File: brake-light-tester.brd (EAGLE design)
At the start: 160 x 100 mm, 24 parts, among them J1 CON_HEADER_PRG_AVR_ICSP-SMD, U1 ATTINY85-20SU, U2 TSL2561FN, U4 LM1117/5V

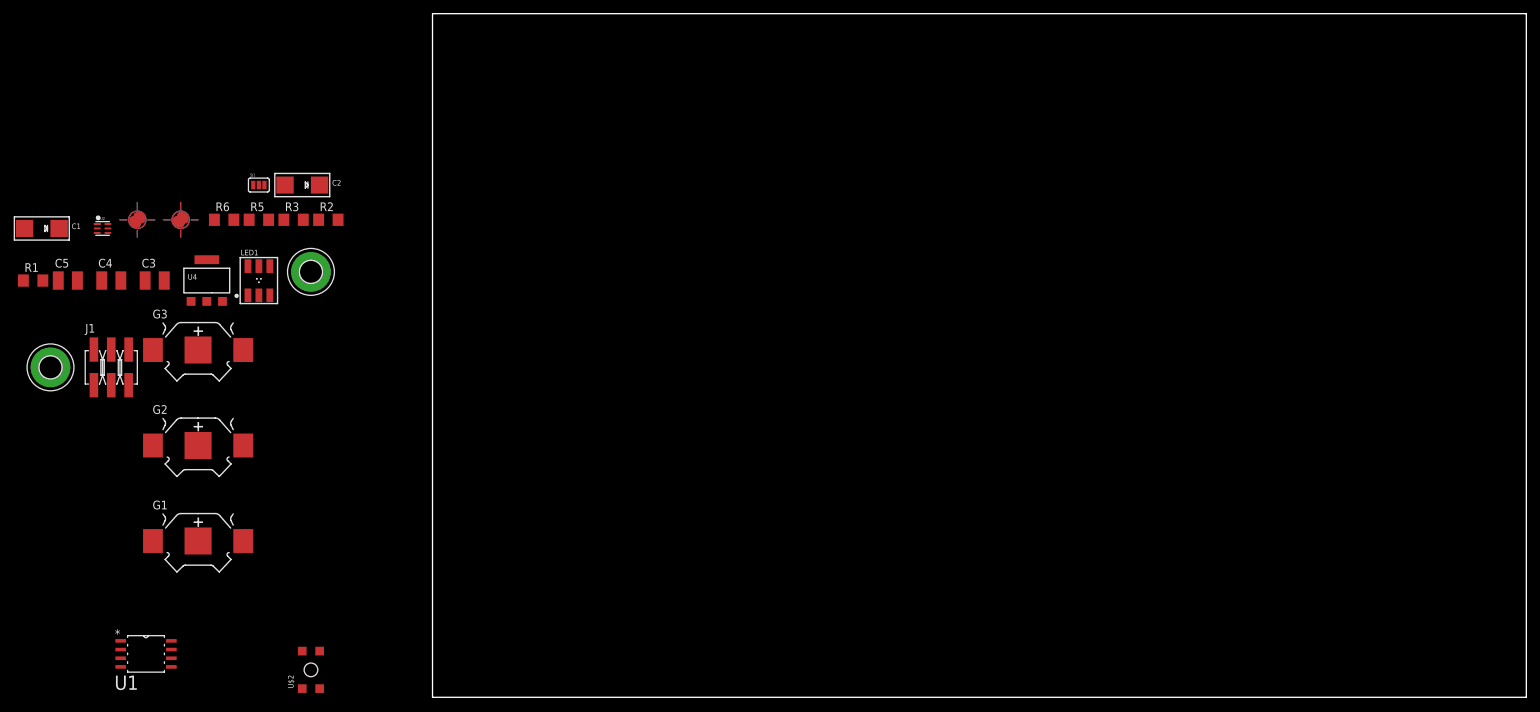
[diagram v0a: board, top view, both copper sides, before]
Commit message: Components laid out but unrouted.
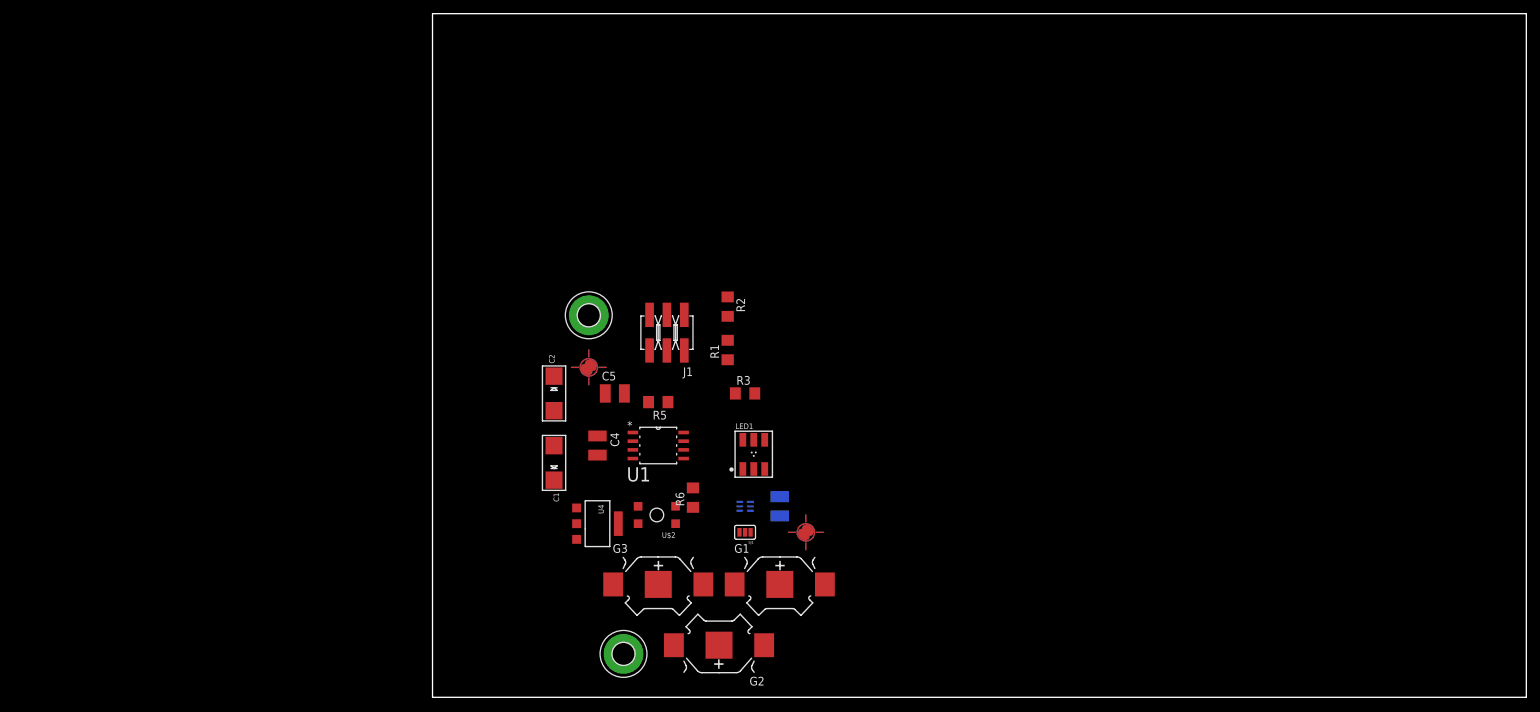
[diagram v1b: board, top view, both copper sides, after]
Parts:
- moved FID2 107.9 mm to (54.6, 24.1)
- moved U2 102.4 mm to (45.7, 27.9), flipped to the bottom
- moved R1 102.1 mm to (43.2, 50.8), turned to 90 degrees
- moved C3 97.2 mm to (50.8, 27.9), flipped to the bottom, turned to 270 degrees
- moved SJ1 87.4 mm to (45.7, 24.1), turned to 180 degrees
- moved G1 85.3 mm to (50.8, 16.5)
- moved C1 82.4 mm to (17.8, 34.3), turned to 270 degrees
- moved C5 81.7 mm to (26.7, 44.5)
- moved G2 81.6 mm to (41.9, 7.62), turned to 180 degrees
- moved J1 81.4 mm to (34.3, 53.3), turned to 180 degrees
- moved U1 80.9 mm to (33.0, 36.8)
- moved R6 79.7 mm to (38.1, 29.2), turned to 90 degrees
- moved H1 79.1 mm to (22.9, 55.9)
- moved LED1 76.7 mm to (47.0, 35.6)
- moved G3 75.5 mm to (33.0, 16.5)
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
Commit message: Manually routed PCB, first iteration.
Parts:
- moved FID2 0.94 mm to (54.8, 25.1)
- turned SJ1 to 0 degrees
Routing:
- net +5V: track 0.00 -> 121.5 mm, vias 0 -> 8
- net GND: track 0.00 -> 104.5 mm, vias 0 -> 5
- net PB2: track 0.00 -> 49.9 mm, vias 0 -> 3
- net PB0: track 0.00 -> 41.3 mm, vias 0 -> 3
- net N$1: track 0.00 -> 37.1 mm
- net PB1: track 0.00 -> 27.1 mm, vias 0 -> 2
- net N$6: track 0.00 -> 26.8 mm
- net N$5: track 0.00 -> 26.2 mm
- net PB5: track 0.00 -> 20.1 mm
- net PB4: track 0.00 -> 19.8 mm
- net N$3: track 0.00 -> 19.1 mm, vias 0 -> 2
- net PB3: track 0.00 -> 11.5 mm, vias 0 -> 2
- net N$2: track 0.00 -> 7.57 mm, vias 0 -> 1
- net N$4: track 0.00 -> 6.84 mm
- net N$7: track 0.00 -> 2.60 mm

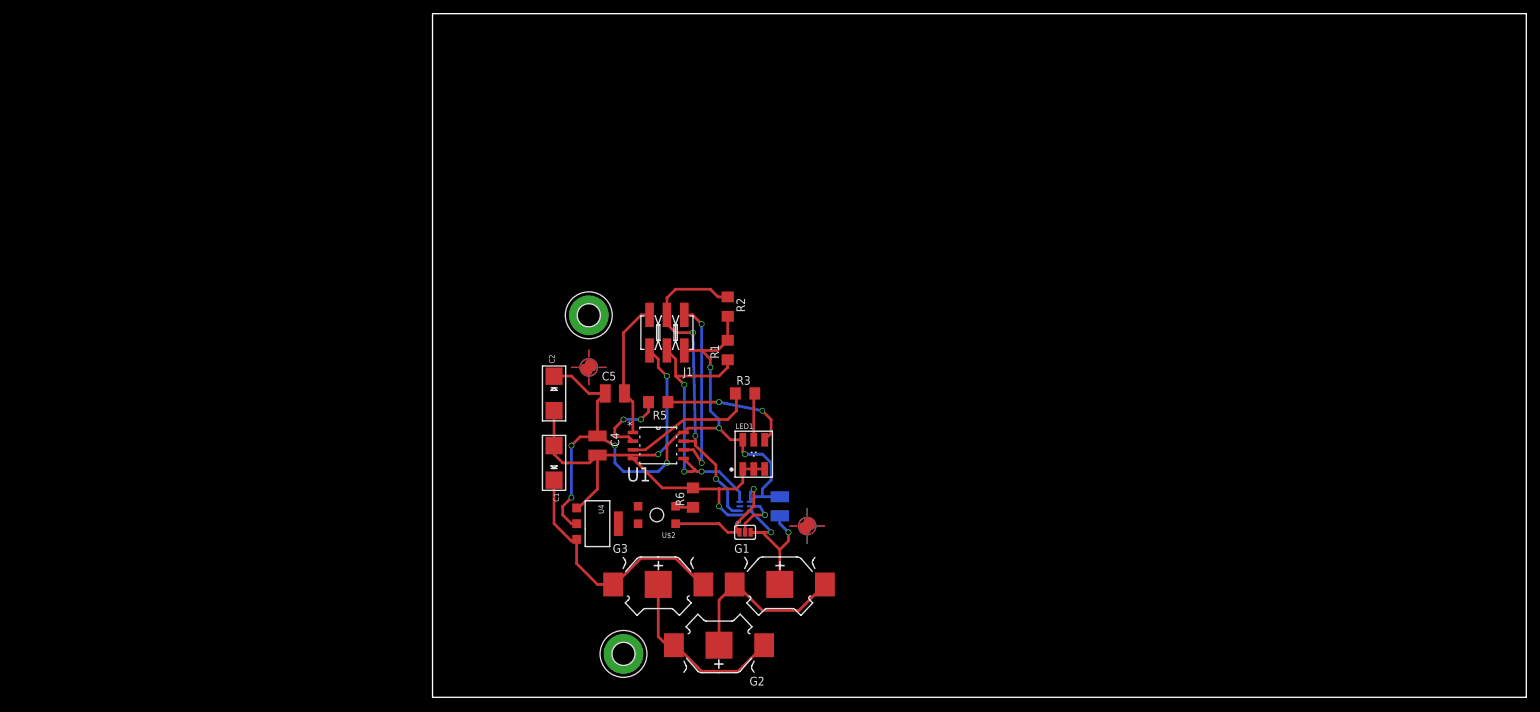
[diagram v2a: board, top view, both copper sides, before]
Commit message: External dimension margins fixed (layer Dimensions).
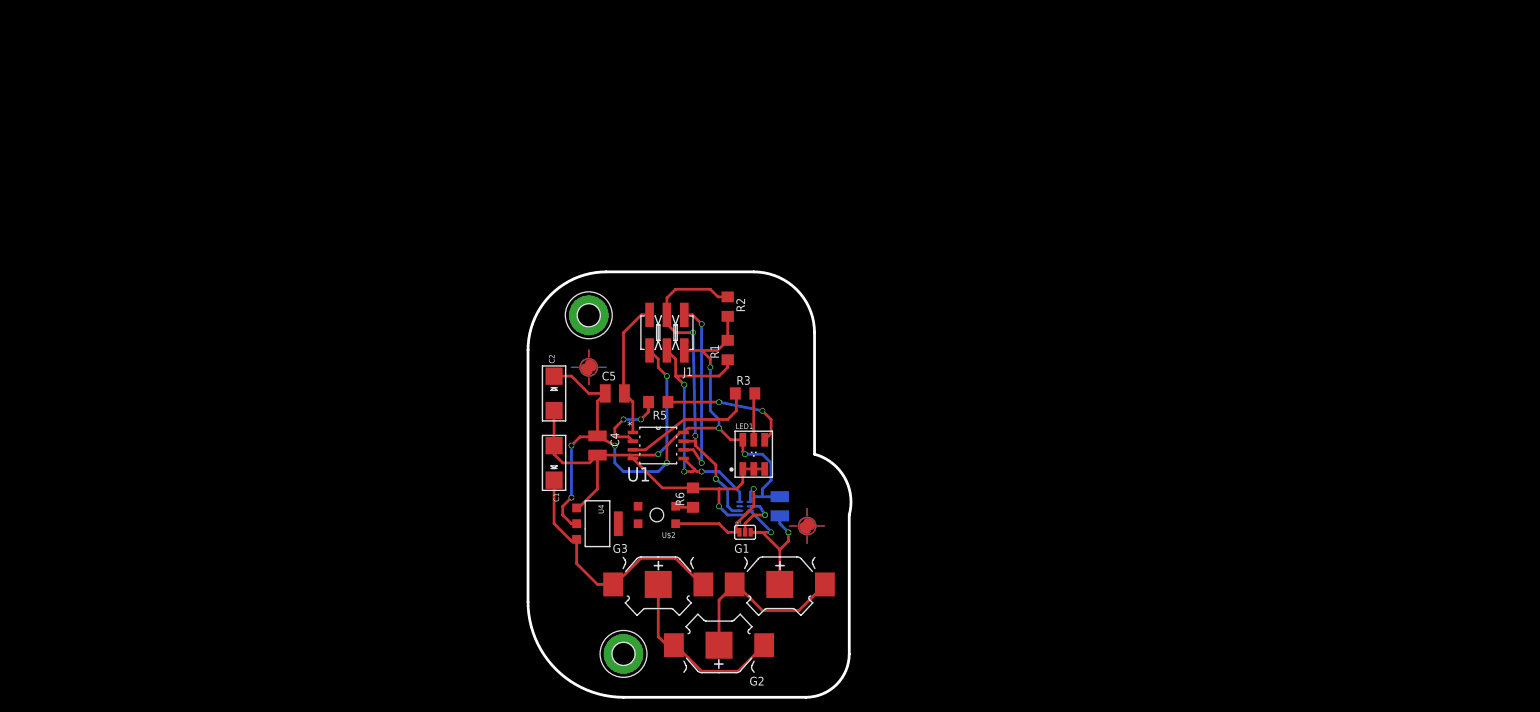
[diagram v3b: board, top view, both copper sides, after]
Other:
- board size 160 x 100 mm -> 47.2 x 62.2 mm
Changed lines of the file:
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@@
 <board>
 <plain>
-<wire x1="0" y1="0" x2="160" y2="0" width="0" layer="20"/>
-<wire x1="160" y1="0" x2="160" y2="100" width="0" layer="20"/>
-<wire x1="160" y1="100" x2="0" y2="100" width="0" layer="20"/>
-<wire x1="0" y1="100" x2="0" y2="0" width="0" layer="20"/>
+<wire x1="27.94" y1="0" x2="13.97" y2="13.97" width="0.4064" layer="20" curve="-90"/>
+<wire x1="13.97" y1="13.97" x2="13.97" y2="50.8" width="0.4064" layer="20"/>
+<wire x1="13.97" y1="50.8" x2="25.4" y2="62.23" width="0.4064" layer="20" curve="-90"/>
+<wire x1="25.4" y1="62.23" x2="46.99" y2="62.23" width="0.4064" layer="20"/>
+<wire x1="46.99" y1="62.23" x2="55.88" y2="53.34" width="0.4064" layer="20" curve="-90"/>
+<wire x1="55.88" y1="53.34" x2="55.88" y2="35.56" width="0.4064" layer="20"/>
+<wire x1="55.88" y1="35.56" x2="60.96" y2="26.67" width="0.4064" layer="20" curve="-90"/>
+<wire x1="60.96" y1="26.67" x2="60.96" y2="6.35" width="0.4064" layer="20"/>
+<wire x1="60.96" y1="6.35" x2="54.61" y2="0" width="0.4064" layer="20" curve="-90"/>
+<wire x1="54.61" y1="0" x2="27.94" y2="0" width="0.4064" layer="20"/>
 </plain>
 <attributes>
